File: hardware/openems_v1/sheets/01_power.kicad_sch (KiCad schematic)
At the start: 0 parts

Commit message: feat(hw): fecha esquemático v2 — sheets 01/02/03/05/07/11 desenhadas, ERC 0
- 01_power: nova — P-FET reverse (Q1) + F1 30A + SMBJ24CA + bulk 100µF/100nF,
  star GND (PGND/SGND/AGND) via PWR_FLAG na sheet produtora, VBAT limpo para
  o resto da placa (buck/LDO ficam no TPS65381A, sheet PMIC)
- 02_ckp / 03_cmp: CKP Hall (espelho do CMP) → MCU.PA0/PA1
- 05_analog: refeita do zero a partir do pinout_v2 (13 canais ADC), mapa
  pré-v2 descartado
- 11_mcu_h562: netlist U1 corrigido (lib_id não resolvia pinos — 100 pinos
  caíam na mesma net); globals PA0/PA1/PB4 sincronizados com as sheets acima
- 07_flex: pino corrigido para PB4 (pinout_v2)
- READMEs (hardware/openems_v1, docs/hw/schematic) actualizados ao estado
  real por sheet

Passos 1-5 do roadmap do esquemático fechados; ERC isolado por sheet em 0
erros (avisos residuais são globals sem sheet destino ainda — esperado).

Co-Authored-By: Claude Sonnet 5 <noreply@anthropic.com>
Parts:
- added C1: 100uF 35V low-ESR, Capacitor_THT:CP_Radial_D8.0mm_P3.50mm, symbol Device:C
- added C2: 100nF 50V, Capacitor_SMD:C_0603_1608Metric, symbol Device:C
- added D1: SMBJ24CA, Diode_SMD:D_SMB, symbol Device:D_TVS
- added F1: 30A, Fuse:Fuseholder_Blade_Mini_Keystone_3568, symbol Device:Fuse
- added Q1: P-MOSFET auto ≥40V (IRF7416 class), Package_TO_SOT_SMD:TO-252-2, symbol Device:Q_PMOS_GSD
- added R1: 100k, Resistor_SMD:R_0603_1608Metric, symbol Device:R
- added R2: 1M (opc.), Resistor_SMD:R_0603_1608Metric, symbol Device:R
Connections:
- new net J2.VBAT+: F1.1
- new net N_Q1_GATE: Q1.1 (G), R1.1, R2.1
- new net PGND: C1.2, C2.2, D1.1 (A1), R1.2
- new net VBAT: C1.1, C2.1, D1.2 (A2), Q1.3 (D)
- new net VBAT_RAW: F1.2, Q1.2 (S), R2.2
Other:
- note added: "Sheet 01 — Power input protection (v2) | VBAT only — PMIC separate"

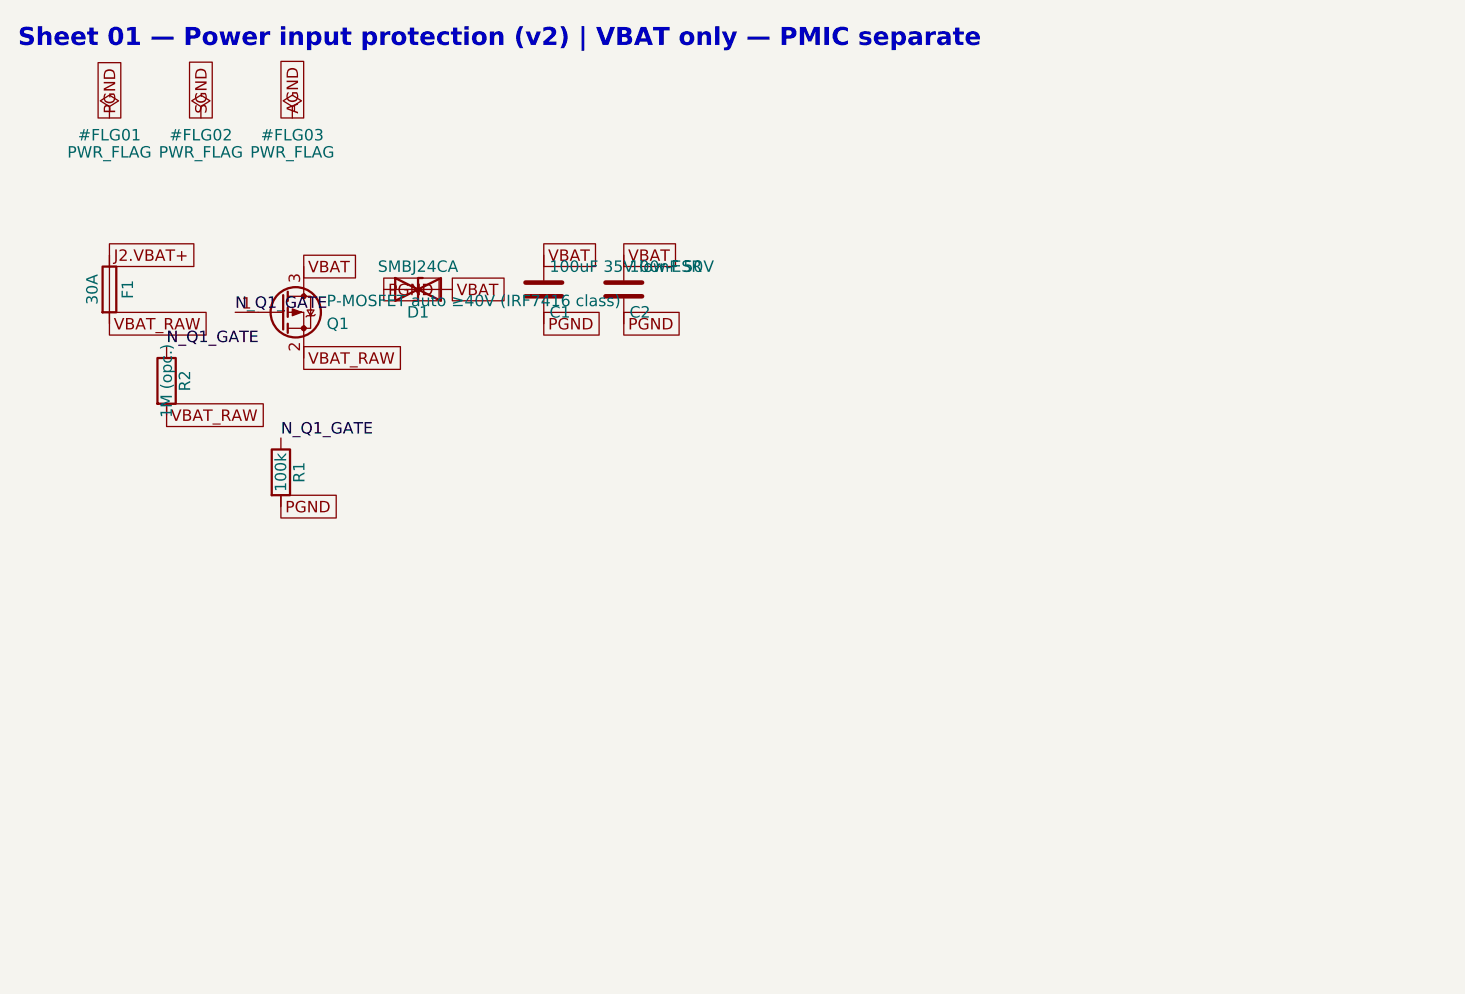
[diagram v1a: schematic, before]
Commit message: fix(hw): corrige legibilidade de 01_power e 02_ckp — layout, não topologia
Render visual (kicad-cli export svg) mostrou os componentes sobrepostos uns
aos outros (D1/C1/C2 e R10/D2 amontoados no canto da folha) apesar do ERC
0 erros — ERC não valida legibilidade, só conectividade. Nenhum bloco
tinha sido efectivamente olhado desde que foi desenhado.

- Pitch entre componentes alargado (10-15mm → 20-35mm)
- Valores do Value field encurtados (o detalhe fica na doc, não no canvas)
- Orientação dos labels ajustada para apontar para fora do corpo do
  símbolo em vez de atravessá-lo (Q1 gate, D1/D2 TVS, C2)
- Conectividade eléctrica idêntica à anterior — só reposicionamento;
  ERC 0 erros mantido nas duas sheets

Co-Authored-By: Claude Sonnet 5 <noreply@anthropic.com>
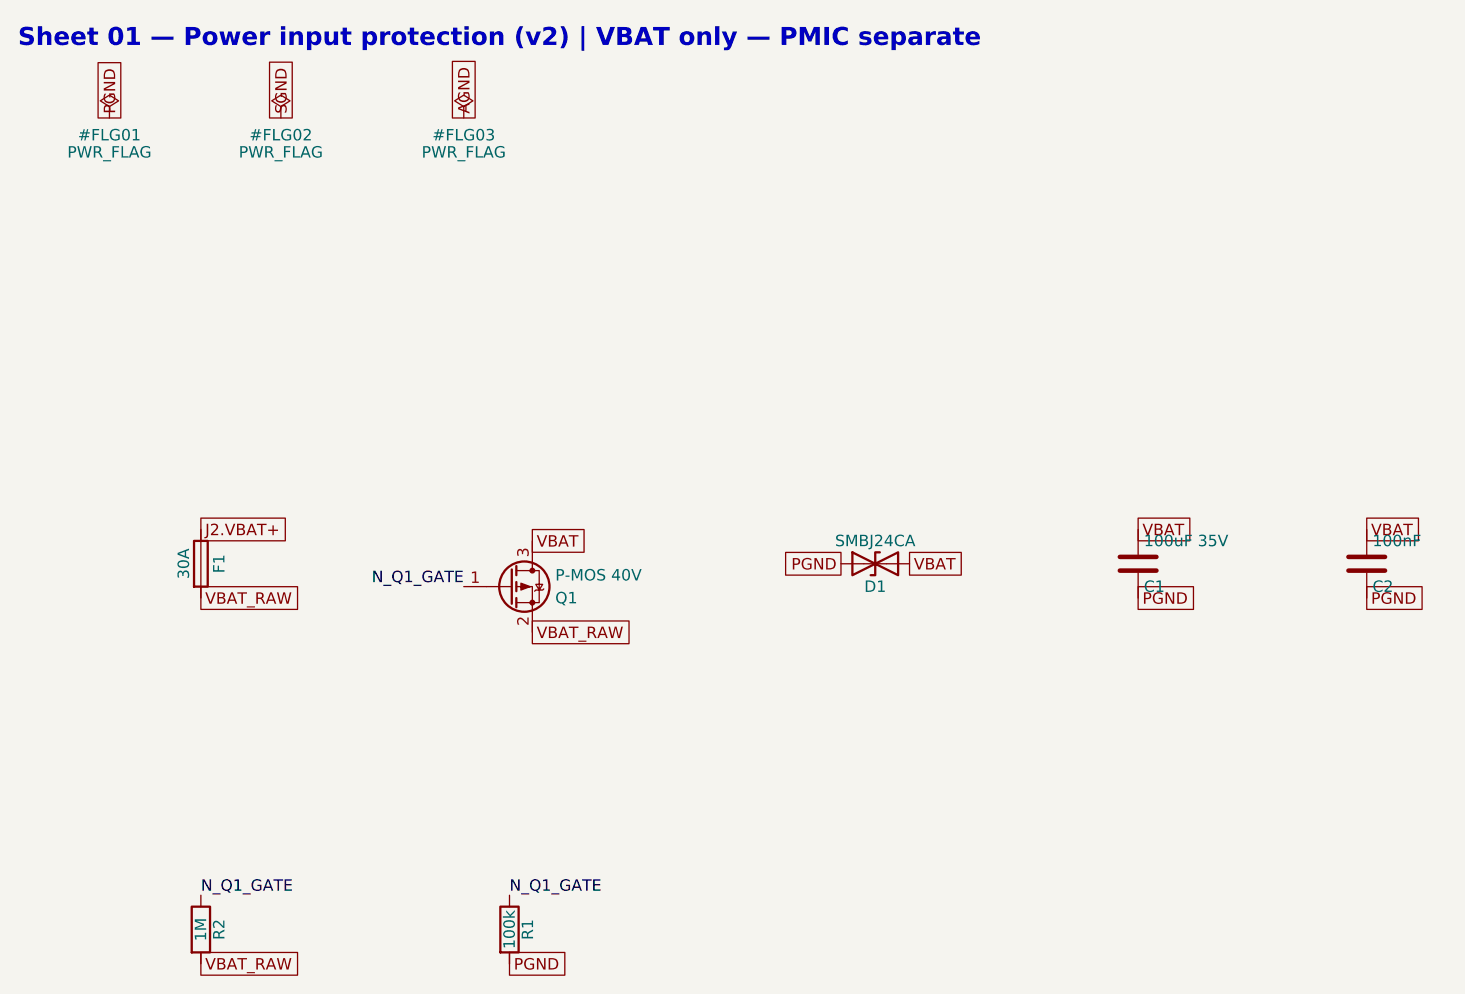
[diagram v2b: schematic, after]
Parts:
- C1: value 100uF 35V low-ESR -> 100uF 35V
- C2: value 100nF 50V -> 100nF
- Q1: value P-MOSFET auto ≥40V (IRF7416 class) -> P-MOS 40V
- R2: value 1M (opc.) -> 1M
